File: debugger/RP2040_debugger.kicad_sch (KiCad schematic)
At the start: 42 parts, among them J1 USB_C_Receptacle_USB2.0, J2 Conn_01x06, J3 Conn_01x06, J4 Conn_01x10, SW1 SW_MEC_5G, U1 W25Q16JVSSIQ, U2 LD1086DT33TR, U3 RP2040, Y1 Crystal_GND24

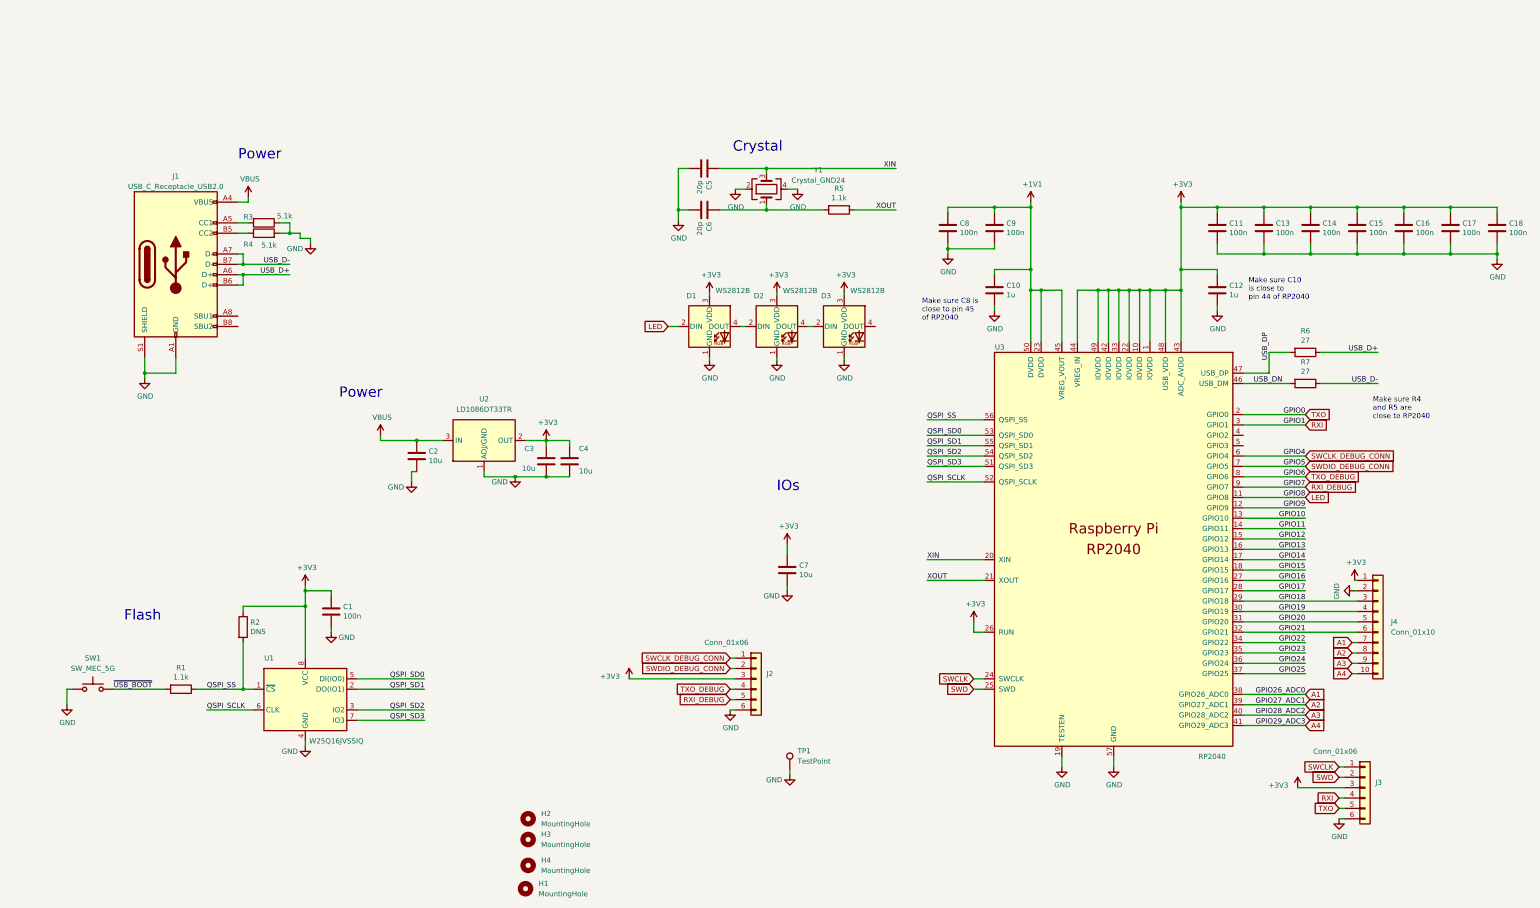
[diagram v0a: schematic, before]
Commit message: Add latest debugger, main board, and new driver module
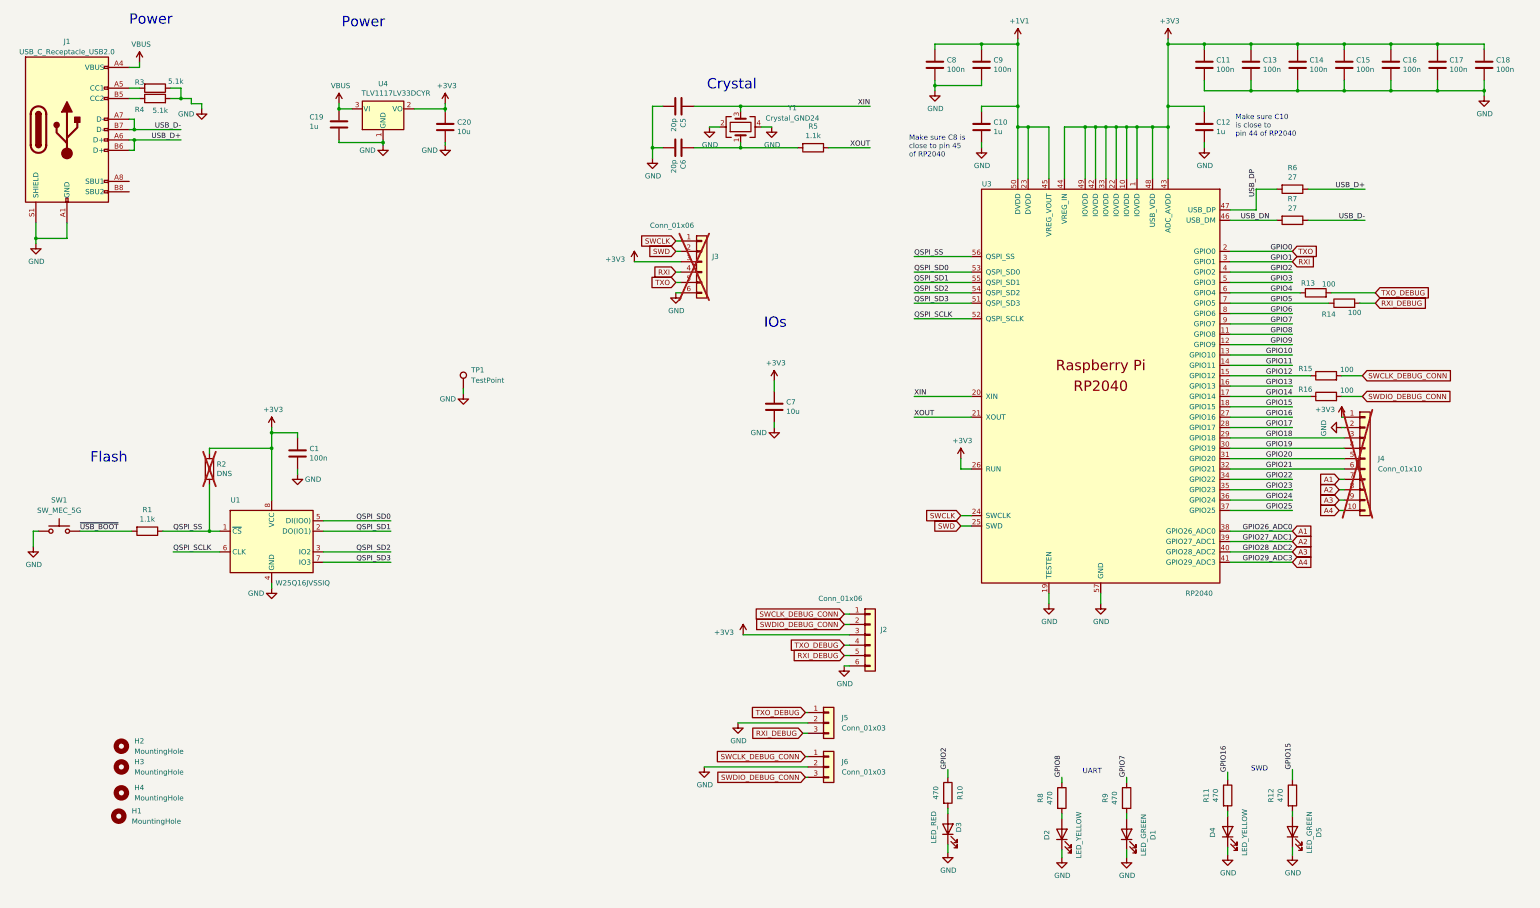
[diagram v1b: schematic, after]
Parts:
- removed C2, C3, C4: 10u, Capacitor_SMD:C_0805_2012Metric, symbol Device:C
- removed D1, D2, D3: WS2812B, RP2040_minimal:LED_WS2812_3528_3.5x2.8mm_P1.5mm, symbol MotorBuck:WS2812B
- removed U2: LD1086DT33TR, Package_TO_SOT_SMD:TO-252-2, symbol Regulator_Linear:LD1086DT33TR
- added C19: 1u, Capacitor_SMD:C_0603_1608Metric, symbol Device:C
- added C20: 10u, Capacitor_SMD:C_0805_2012Metric, symbol Device:C
- added D1, D5: LED_GREEN, LED_SMD:LED_0805_2012Metric, symbol Device:LED
- added D2, D4: LED_YELLOW, LED_SMD:LED_0805_2012Metric, symbol Device:LED
- added D3: LED_RED, LED_SMD:LED_0805_2012Metric, symbol Device:LED
- added J5, J6: Conn_01x03, Connector_JST:JST_SH_SM03B-SRSS-TB_1x03-1MP_P1.00mm_Horizontal, symbol Connector_Generic:Conn_01x03
- added R10, R11, R12, R8, R9: 470, Resistor_SMD:R_0603_1608Metric, symbol Device:R
- added R13, R14, R15, R16: 100, Resistor_SMD:R_0603_1608Metric, symbol Device:R
- added U4: TLV1117LV33DCYR, Package_TO_SOT_SMD:SOT-223-3_TabPin2, symbol Regulator_Linear:NCP1117-3.3_SOT223
- J3, R2: now not fitted; now left out of the parts list
- J4: now not fitted
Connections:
- net +3V3: now also C20.1, U4.2 (VO)
- net GND: now also C19.2, C20.2, D1.1 (K), D2.1 (K), D3.1 (K), D4.1 (K), D5.1 (K), J5.2 (Pin_2), J6.2 (Pin_2), U4.1 (GND)
- net GPIO12: now also R15.1
- net GPIO14: now also R16.1
- net GPIO15: now also R12.1
- net GPIO16: now also R11.1
- net RXI_DEBUG: now also J5.3 (Pin_3), R14.2; no longer U3.9 (GPIO7)
- net SWCLK_DEBUG_CONN: now also J6.1 (Pin_1), R15.2; no longer U3.6 (GPIO4)
- net SWDIO_DEBUG_CONN: now also J6.3 (Pin_3), R16.2; no longer U3.7 (GPIO5)
- net TXO_DEBUG: now also J5.1 (Pin_1), R13.2; no longer U3.8 (GPIO6)
- net VBUS: now also C19.1, U4.3 (VI)
- net GPIO2: now reaches U3.4 (GPIO2)
- net GPIO2: now also R10.1
- net GPIO3: now reaches U3.5 (GPIO3)
- net LED renamed GPIO8
- net GPIO8: now also R8.1
- new net: D5.2 (A), R12.2
- new net: D3.2 (A), R10.2
- new net: D4.2 (A), R11.2
- new net: D2.2 (A), R8.2
- new net: D1.2 (A), R9.2
- new net GPIO4: R13.1, U3.6 (GPIO4)
- new net GPIO5: R14.1, U3.7 (GPIO5)
- new net GPIO6: U3.8 (GPIO6)
- new net GPIO7: R9.1, U3.9 (GPIO7)
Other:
- note added: "SWD"
- note added: "UART"
- note removed: "Make sure R4 and R5 are close to RP2040"
- moved on the sheet: C1, C10, C11, C12, C13, C14, C15, C16, C17, C18, C5, C6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

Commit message: Debugger: Separated target power, added led switch, fix firmware buffered pins issue .
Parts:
- added C2: 1u, Capacitor_SMD:C_0603_1608Metric, symbol Device:C
- added C21, C4: 100u, Capacitor_SMD:C_1206_3216Metric, symbol Device:C
- added C3: 10u, Capacitor_SMD:C_0805_2012Metric, symbol Device:C
- added Q1: Q_NMOS_GSD, Package_TO_SOT_SMD:SOT-23, symbol Device:Q_NMOS_GSD
- added R17: 5.1k, Resistor_SMD:R_0603_1608Metric, symbol Device:R
- added SW2: SW_DIP_x01, base_parts:SW-SMD_DSHP01TSGER, symbol Switch:SW_DIP_x01
- added U2: TLV1117LV33DCYR, Package_TO_SOT_SMD:SOT-223-3_TabPin2, symbol Regulator_Linear:NCP1117-3.3_SOT223
- J3: now fitted; now in the parts list
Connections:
- net GPIO14 is gone; now on net GPIO13: R16.1, U3.17 (GPIO14)
- net GPIO6 is gone; now on net GPIO5: U3.8 (GPIO6)
- net +3V3: now also C21.1, SW2.1; no longer J2.3 (Pin_3)
- net GND: now also C2.2, C21.2, C3.2, C4.2, Q1.2 (S), R17.2, U2.1 (GND); no longer D1.1 (K), D2.1 (K), D3.1 (K), D4.1 (K), D5.1 (K)
- net VBUS: now also C2.1, U2.3 (VI)
- new net: Q1.1 (G), R17.1, SW2.2
- new net 3.3V_OUT: C3.1, C4.1, J2.3 (Pin_3), U2.2 (VO)
- new net LED_GND: D1.1 (K), D2.1 (K), D3.1 (K), D4.1 (K), D5.1 (K), Q1.3 (D)
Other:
- moved on the sheet: D1, D2, D4, D5, R11, R12, R8, R9

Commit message: Updated files for boards ordered July 2024
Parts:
- added J10, J7, J8, J9: Conn_01x01, TestPoint:TestPoint_Keystone_5019_Minature, symbol Connector_Generic:Conn_01x01
- TP1: LCSC C238130 -> C238131; MPN (none) -> 5019
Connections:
- net GND: now also J10.1 (Pin_1)
- net VBUS: now also J7.1 (Pin_1)
- net GPIO11 renamed AUX_SCK
- net AUX_SCK: now also J9.1 (Pin_1)
- net GPIO3 renamed AUX_TX
- net AUX_TX: now also J8.1 (Pin_1)
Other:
- moved on the sheet: C1, C10, C11, C12, C13, C14, C15, C16, C17, C18, C19, C2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
